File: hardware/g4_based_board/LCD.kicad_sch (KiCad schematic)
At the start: 18 parts, among them Q4 BC547, U11 TXS0102DCT, U12 PCF8574

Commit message: added docs
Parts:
- C33, C34, C35, C36, C37: footprint Capacitor_SMD:C_0805_2012Metric -> Capacitor_SMD:C_0603_1608Metric_Pad1.08x0.95mm_HandSolder
- JP15, JP16, JP17: footprint (none) -> Jumper:SolderJumper-3_P1.3mm_Open_RoundedPad1.0x1.5mm
- JP18, JP19: footprint (none) -> Jumper:SolderJumper-2_P1.3mm_Open_TrianglePad1.0x1.5mm
- R29, R30, R31: footprint Resistor_SMD:R_0805_2012Metric -> Resistor_SMD:R_0603_1608Metric_Pad0.98x0.95mm_HandSolder

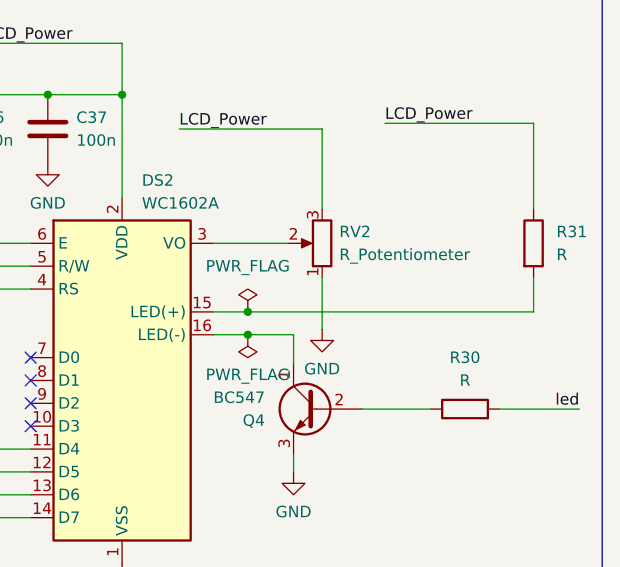
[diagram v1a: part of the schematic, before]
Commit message: added values to resistors
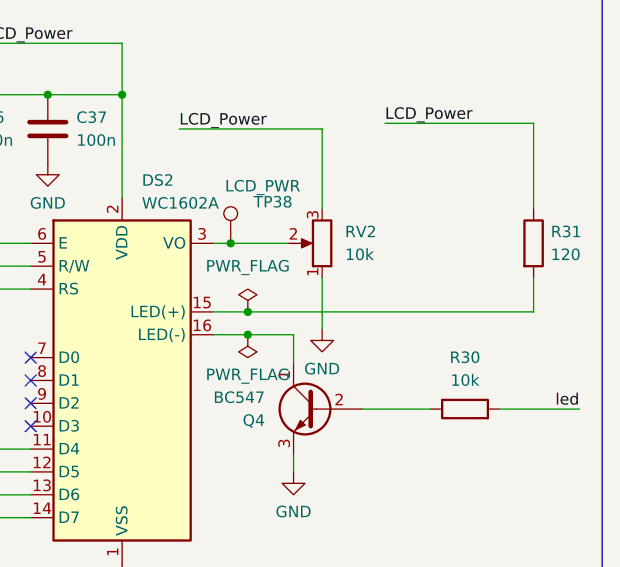
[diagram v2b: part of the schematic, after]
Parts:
- added TP38: LCD_PWR, TestPoint:TestPoint_Pad_D1.5mm, symbol Connector:TestPoint
- Q4: footprint Package_TO_SOT_THT:TO-92_Inline -> Package_TO_SOT_SMD:SOT-23-3
- R30: value R -> 10k
- R31: value R -> 120
- RV2: value R_Potentiometer -> 10k
- U12: footprint Package_SO:SOIC-16W-12_7.5x10.3mm_P1.27mm -> Package_SO:SOIC-16W_7.5x10.3mm_P1.27mm
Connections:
- net at DS2.3 (VO), RV2.2: now also TP38.1
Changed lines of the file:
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@@
 	)
 	(junction
+		(at 238.76 112.395)
+		(diameter 0)
+		(color 0 0 0 0)
+	)
+	(junction
 		(at 250.19 50.165)
 		(diameter 0)
@@
 	(wire
 		(pts
+			(xy 238.76 112.395) (xy 245.11 112.395)
+		)
+		(stroke
+			(width 0)
+			(type default)
+		)
+	)
+	(wire
+		(pts
 			(xy 100.33 122.555) (xy 108.585 122.555)
 		)
@@
 	(wire
 		(pts
-			(xy 236.855 112.395) (xy 245.11 112.395)
+			(xy 236.855 112.395) (xy 238.76 112.395)
 		)
 		(stroke
@@
 	)
 	(symbol
+		(lib_id "Connector:TestPoint")
+		(at 238.76 112.395 0)
+		(unit 1)
+		(exclude_from_sim no)
+		(in_bom yes)
+		(on_board yes)
+		(dnp no)
+		(property "Reference" "TP38"
+			(at 241.3 107.8229 0)
+			(effects
+				(font
+					(size 1.27 1.27)
+				)
+				(justify left)
+			)
+		)
+		(property "Value" "LCD_PWR"
+			(at 238.125 106.045 0)
+			(effects
+				(font
+					(size 1.27 1.27)
+				)
+				(justify left)
+			)
+		)
+		(property "Footprint" "TestPoint:TestPoint_Pad_D1.5mm"
+			(at 243.84 112.395 0)
+			(effects
+				(font
+					(size 1.27 1.27)
+				)
+				(hide yes)
+			)
+		)
+		(property "Datasheet" "~"
+			(at 243.84 112.395 0)
+			(effects
+				(font
+					(size 1.27 1.27)
+				)
+				(hide yes)
+			)
+		)
+		(property "Description" ""
+			(at 238.76 112.395 0)
+			(effects
+				(font
+					(size 1.27 1.27)
+				)
+				(hide yes)
+			)
+		)
+		(pin "1"
+		)
+		(instances
+			(project "data_logger"
+				(path "/9bc93932-ff5f-4f35-96cf-dfa5f042acb6/d4605b59-911a-47dc-8072-99de95361456/b23c49c6-61fc-48c4-8510-95e902e0d831"
+					(reference "TP38")
+					(unit 1)
+				)
+			)
+		)
+	)
+	(symbol
 		(lib_name "GND_3")
 		(lib_id "power:GND")
@@
 			)
 		)
-		(property "Footprint" "Package_SO:SOIC-16W-12_7.5x10.3mm_P1.27mm"
+		(property "Footprint" "Package_SO:SOIC-16W_7.5x10.3mm_P1.27mm"
 			(at 87.63 125.095 0)
 			(effects
@@
 			)
 		)
+		(property "Name" ""
+			(at 87.63 125.095 0)
+			(effects
+				(font
+					(size 1.27 1.27)
+				)
+			)
+		)
 		(pin "3"
 		)
@@
 			)
 		)
-		(property "Value" "R"
+		(property "Value" "10k"
 			(at 264.795 127.635 90)
 			(effects
@@
 			)
 		)
+		(property "Name" ""
+			(at 264.795 130.81 0)
+			(effects
+				(font
+					(size 1.27 1.27)
+				)
+			)
+		)
 		(pin "1"
 		)
@@
 		(fields_autoplaced yes)
 		(property "Reference" "R31"
-			(at 274.955 111.1249 0)
+			(at 274.32 111.1249 0)
 			(effects
 				(font
@@
 			)
 		)
-		(property "Value" "R"
-			(at 274.955 113.6649 0)
+		(property "Value" "120"
+			(at 274.32 113.6649 0)
 			(effects
 				(font
@@
 			)
 		)
-		(property "Footprint" "Package_TO_SOT_THT:TO-92_Inline"
+		(property "Footprint" "Package_TO_SOT_SMD:SOT-23-3"
 			(at 243.205 132.715 0)
 			(effects
@@
 			)
 		)
+		(property "Name" ""
+			(at 248.285 130.81 0)
+			(effects
+				(font
+					(size 1.27 1.27)
+				)
+			)
+		)
 		(pin "2"
 		)
@@
 		(fields_autoplaced yes)
 		(property "Reference" "RV2"
-			(at 250.825 111.1249 0)
+			(at 251.46 111.1249 0)
 			(effects
 				(font
@@
 			)
 		)
-		(property "Value" "R_Potentiometer"
-			(at 250.825 113.6649 0)
+		(property "Value" "10k"
+			(at 251.46 113.6649 0)
 			(effects
 				(font

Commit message: auto updated
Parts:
- renumbered C33 to C21, C34 to C22, C35 to C23, C36 to C24, C37 to C25, DS2 to DS1, JP15 to JP20, JP16 to JP21, JP17 to JP22, JP18 to JP23, JP19 to JP24, Q4 to Q5, R29 to R19, R30 to R20, R31 to R21, RV2 to RV1, TP38 to TP5, U11 to U4, U12 to U5

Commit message: rev-1
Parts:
- removed C21, C22, C23, C24, C25: 100n, Capacitor_SMD:C_0603_1608Metric_Pad1.08x0.95mm_HandSolder, symbol Device:C
- removed DS1: WC1602A, Display:WC1602A, symbol Display_Character:WC1602A
- removed JP20, JP21, JP22: SolderJumper_3_Open, Jumper:SolderJumper-3_P1.3mm_Open_RoundedPad1.0x1.5mm, symbol Jumper:SolderJumper_3_Open
- removed JP23, JP24: Jumper_2_Open, Jumper:SolderJumper-2_P1.3mm_Open_TrianglePad1.0x1.5mm, symbol Jumper:Jumper_2_Open
- removed Q5: BC547, Package_TO_SOT_SMD:SOT-23-3, symbol Transistor_BJT:BC547
- removed R19, R20: 10k, Resistor_SMD:R_0603_1608Metric_Pad0.98x0.95mm_HandSolder, symbol Device:R
- removed R21: 120, Resistor_SMD:R_0603_1608Metric_Pad0.98x0.95mm_HandSolder, symbol Device:R
- removed RV1: 10k, Potentiometer_THT:Potentiometer_Vishay_T73XX_Horizontal, symbol Device:R_Potentiometer
- removed TP5: LCD_PWR, TestPoint:TestPoint_Pad_D1.5mm, symbol Connector:TestPoint
- removed U4: TXS0102DCT, Package_SO:SSOP-8_2.95x2.8mm_P0.65mm, symbol Logic_LevelTranslator:TXS0102DCT
- removed U5: PCF8574, Package_SO:SOIC-16W_7.5x10.3mm_P1.27mm, symbol Interface_Expansion:PCF8574
- added J4: Conn_01x04, Connector_Molex:Molex_KK-254_AE-6410-04A_1x04_P2.54mm_Vertical, symbol Connector_Generic:Conn_01x04
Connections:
- net +3.3V: now also J4.3 (Pin_3)
- net GND: now also J4.4 (Pin_4)
- net SCL: now also J4.1 (Pin_1)
- net SDA: now also J4.2 (Pin_2)
- no-connect marks 5 -> 0
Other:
- note added: "https://www.sparkfun.com/products/24606"
- note removed: "I2C port expander"
- note removed: "LCD"
- note removed: "LOGIC LEVEL SHIFTER"
- note removed: "POWER JUMPER so the whole module doesnt have to be powered"
